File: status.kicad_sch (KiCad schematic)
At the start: 10 parts

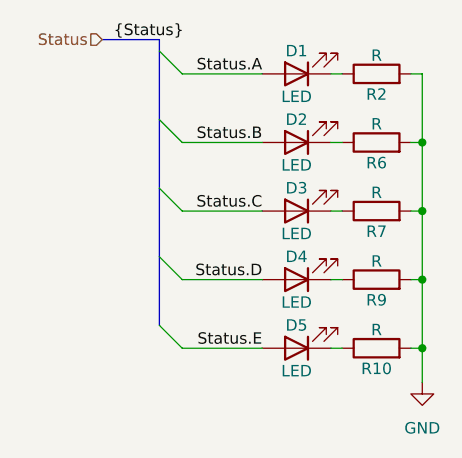
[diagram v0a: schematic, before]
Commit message: LED descriptions - Status LEDs could use some more work
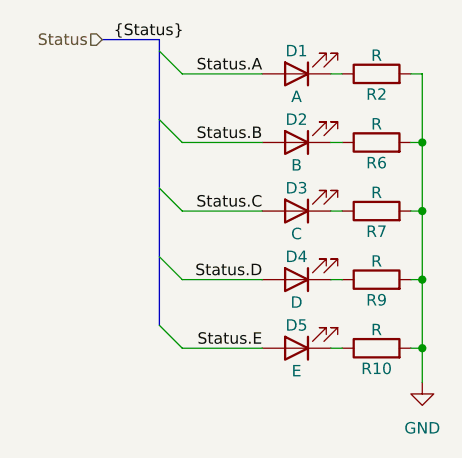
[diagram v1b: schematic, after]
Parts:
- D1: value LED -> A
- D2: value LED -> B
- D3: value LED -> C
- D4: value LED -> D
- D5: value LED -> E
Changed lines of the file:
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@@
 			)
 		)
-		(property "Value" "LED"
+		(property "Value" "B"
 			(at 140.97 95.25 0)
 			(effects
@@
 			)
 		)
-		(property "Value" "LED"
+		(property "Value" "C"
 			(at 140.97 102.87 0)
 			(effects
@@
 			)
 		)
-		(property "Value" "LED"
+		(property "Value" "E"
 			(at 140.97 118.11 0)
 			(effects
@@
 			)
 		)
-		(property "Value" "LED"
+		(property "Value" "D"
 			(at 140.97 110.49 0)
 			(effects
@@
 			)
 		)
-		(property "Value" "LED"
+		(property "Value" "A"
 			(at 140.97 87.63 0)
 			(effects

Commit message: Initial component placement
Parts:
- D1, D2, D3, D4, D5: footprint (none) -> LED_SMD:LED_0805_2012Metric_Pad1.15x1.40mm_HandSolder
- R10, R2, R6, R7, R9: footprint (none) -> Resistor_SMD:R_0805_2012Metric_Pad1.20x1.40mm_HandSolder
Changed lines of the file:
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@@
 			)
 		)
-		(property "Footprint" ""
+		(property "Footprint" "LED_SMD:LED_0805_2012Metric_Pad1.15x1.40mm_HandSolder"
 			(at 140.97 92.71 0)
 			(effects
@@
 			)
 		)
-		(property "Footprint" ""
+		(property "Footprint" "Resistor_SMD:R_0805_2012Metric_Pad1.20x1.40mm_HandSolder"
 			(at 149.86 117.348 90)
 			(effects
@@
 			)
 		)
-		(property "Footprint" ""
+		(property "Footprint" "Resistor_SMD:R_0805_2012Metric_Pad1.20x1.40mm_HandSolder"
 			(at 149.86 102.108 90)
 			(effects
@@
 			)
 		)
-		(property "Footprint" ""
+		(property "Footprint" "Resistor_SMD:R_0805_2012Metric_Pad1.20x1.40mm_HandSolder"
 			(at 149.86 94.488 90)
 			(effects
@@
 			)
 		)
-		(property "Footprint" ""
+		(property "Footprint" "Resistor_SMD:R_0805_2012Metric_Pad1.20x1.40mm_HandSolder"
 			(at 149.86 86.868 90)
 			(effects
@@
 			)
 		)
-		(property "Footprint" ""
+		(property "Footprint" "Resistor_SMD:R_0805_2012Metric_Pad1.20x1.40mm_HandSolder"
 			(at 149.86 109.728 90)
 			(effects
@@
 		(dnp no)
 		(fields_autoplaced yes)
-		(property "Reference" "#PWR016"
+		(property "Reference" "#PWR0101"
 			(at 154.94 125.73 0)
 			(effects
@@
 			(project "LifeCounter"
 				(path "/16b3e55a-9d75-49bf-a6fe-25414eb3d7da/2d968151-724a-4d29-815f-dbf368373ff9"
+					(reference "#PWR0101")
+					(unit 1)
+				)
+				(path "/16b3e55a-9d75-49bf-a6fe-25414eb3d7da/8c2171b0-d87d-41f8-af80-94d86e99ac21"
 					(reference "#PWR016")
 					(unit 1)
@@
 			)
 		)
-		(property "Footprint" ""
+		(property "Footprint" "LED_SMD:LED_0805_2012Metric_Pad1.15x1.40mm_HandSolder"
 			(at 140.97 100.33 0)
 			(effects
@@
 			)
 		)
-		(property "Footprint" ""
+		(property "Footprint" "LED_SMD:LED_0805_2012Metric_Pad1.15x1.40mm_HandSolder"
 			(at 140.97 115.57 0)
 			(effects
@@
 			)
 		)
-		(property "Footprint" ""
+		(property "Footprint" "LED_SMD:LED_0805_2012Metric_Pad1.15x1.40mm_HandSolder"
 			(at 140.97 107.95 0)
 			(effects
@@
 			)
 		)
-		(property "Footprint" ""
+		(property "Footprint" "LED_SMD:LED_0805_2012Metric_Pad1.15x1.40mm_HandSolder"
 			(at 140.97 85.09 0)
 			(effects

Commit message: Initial layout
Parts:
- renumbered D4 to D14, D5 to D15, D1 to D6, D2 to D7, D3 to D8, R2 to R26, R6 to R27, R7 to R28, R9 to R29, R10 to R30
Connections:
- net Status.A renamed A
- net Status.B renamed B
- net Status.C renamed C
- net Status.D renamed D
- net Status.E renamed E
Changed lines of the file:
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@@
 	)
 	(bus_entry
-		(at 125.73 97.79)
+		(at 132.08 97.79)
 		(size 2.54 2.54)
 		(stroke
@@
 	)
 	(bus_entry
-		(at 125.73 82.55)
+		(at 132.08 82.55)
 		(size 2.54 2.54)
 		(stroke
@@
 	)
 	(bus_entry
-		(at 125.73 113.03)
+		(at 132.08 113.03)
 		(size 2.54 2.54)
 		(stroke
@@
 	)
 	(bus_entry
-		(at 125.73 105.41)
+		(at 132.08 105.41)
 		(size 2.54 2.54)
 		(stroke
@@
 	)
 	(bus_entry
-		(at 125.73 90.17)
+		(at 132.08 90.17)
 		(size 2.54 2.54)
 		(stroke
@@
 	(wire
 		(pts
-			(xy 128.27 85.09) (xy 137.16 85.09)
+			(xy 134.62 85.09) (xy 137.16 85.09)
 		)
 		(stroke
@@
 	(wire
 		(pts
-			(xy 128.27 100.33) (xy 137.16 100.33)
-		)
-		(stroke
-			(width 0)
-			(type default)
-		)
-	)
-	(wire
-		(pts
-			(xy 128.27 107.95) (xy 137.16 107.95)
+			(xy 134.62 100.33) (xy 137.16 100.33)
+		)
+		(stroke
+			(width 0)
+			(type default)
+		)
+	)
+	(wire
+		(pts
+			(xy 134.62 107.95) (xy 137.16 107.95)
 		)
 		(stroke
@@
 	(wire
 		(pts
-			(xy 128.27 92.71) (xy 137.16 92.71)
+			(xy 134.62 92.71) (xy 137.16 92.71)
 		)
 		(stroke
@@
 	(bus
 		(pts
-			(xy 119.38 81.28) (xy 125.73 81.28)
+			(xy 125.73 81.28) (xy 132.08 81.28)
 		)
 		(stroke
@@
 	(bus
 		(pts
-			(xy 125.73 82.55) (xy 125.73 90.17)
+			(xy 132.08 82.55) (xy 132.08 90.17)
 		)
 		(stroke
@@
 	(bus
 		(pts
-			(xy 125.73 105.41) (xy 125.73 113.03)
+			(xy 132.08 105.41) (xy 132.08 113.03)
 		)
 		(stroke
@@
 	(bus
 		(pts
-			(xy 125.73 97.79) (xy 125.73 105.41)
+			(xy 132.08 97.79) (xy 132.08 105.41)
 		)
 		(stroke
@@
 	(bus
 		(pts
-			(xy 125.73 81.28) (xy 125.73 82.55)
-		)
-		(stroke
-			(width 0)
-			(type default)
-		)
-	)
-	(wire
-		(pts
-			(xy 128.27 115.57) (xy 137.16 115.57)
+			(xy 132.08 81.28) (xy 132.08 82.55)
+		)
+		(stroke
+			(width 0)
+			(type default)
+		)
+	)
+	(wire
+		(pts
+			(xy 134.62 115.57) (xy 137.16 115.57)
 		)
 		(stroke
@@
 	(bus
 		(pts
-			(xy 125.73 90.17) (xy 125.73 97.79)
+			(xy 132.08 90.17) (xy 132.08 97.79)
 		)
 		(stroke
@@
 		)
 	)
-	(label "Status.A"
+	(label "A"
 		(at 137.16 85.09 180)
 		(fields_autoplaced yes)
@@
 		)
 	)
-	(label "Status.E"
+	(label "E"
 		(at 137.16 115.57 180)
 		(fields_autoplaced yes)
@@
 		)
 	)
-	(label "Status.D"
+	(label "D"
 		(at 137.16 107.95 180)
 		(fields_autoplaced yes)
@@
 		)
 	)
-	(label "Status.C"
+	(label "C"
 		(at 137.16 100.33 180)
 		(fields_autoplaced yes)
@@
 	)
 	(label "{Status}"
-		(at 120.65 81.28 0)
+		(at 127 81.28 0)
 		(fields_autoplaced yes)
 		(effects
@@
 		)
 	)
-	(label "Status.B"
+	(label "B"
 		(at 137.16 92.71 180)
 		(fields_autoplaced yes)
@@
 	(hierarchical_label "Status"
 		(shape input)
-		(at 119.38 81.28 180)
+		(at 125.73 81.28 180)
 		(fields_autoplaced yes)
 		(effects
@@
 		(on_board yes)
 		(dnp no)
-		(property "Reference" "D2"
+		(property "Reference" "D7"
 			(at 140.97 90.17 0)
 			(effects
@@
 		(on_board yes)
 		(dnp no)
-		(property "Reference" "R10"
+		(property "Reference" "R30"
 			(at 149.86 117.856 90)
 			(effects
@@
 		(on_board yes)
 		(dnp no)
-		(property "Reference" "R7"
+		(property "Reference" "R28"
 			(at 149.86 102.616 90)
 			(effects
@@
 		(on_board yes)
 		(dnp no)
-		(property "Reference" "R6"
+		(property "Reference" "R27"
 			(at 149.86 94.996 90)
 			(effects
@@
 		(on_board yes)
 		(dnp no)
-		(property "Reference" "R2"
+		(property "Reference" "R26"
 			(at 149.86 87.376 90)
 			(effects
@@
 		(on_board yes)
 		(dnp no)
-		(property "Reference" "R9"
+		(property "Reference" "R29"
 			(at 149.86 110.236 90)
 			(effects
@@
 		(on_board yes)
 		(dnp no)
-		(property "Reference" "D3"
+		(property "Reference" "D8"
 			(at 140.97 97.79 0)
 			(effects
@@
 		(on_board yes)
 		(dnp no)
-		(property "Reference" "D5"
+		(property "Reference" "D15"
 			(at 140.97 113.03 0)
 			(effects
@@
 		(on_board yes)
 		(dnp no)
-		(property "Reference" "D4"
+		(property "Reference" "D14"
 			(at 140.97 105.41 0)
 			(effects
@@
 		(on_board yes)
 		(dnp no)
-		(property "Reference" "D1"
+		(property "Reference" "D6"
 			(at 140.97 82.55 0)
 			(effects

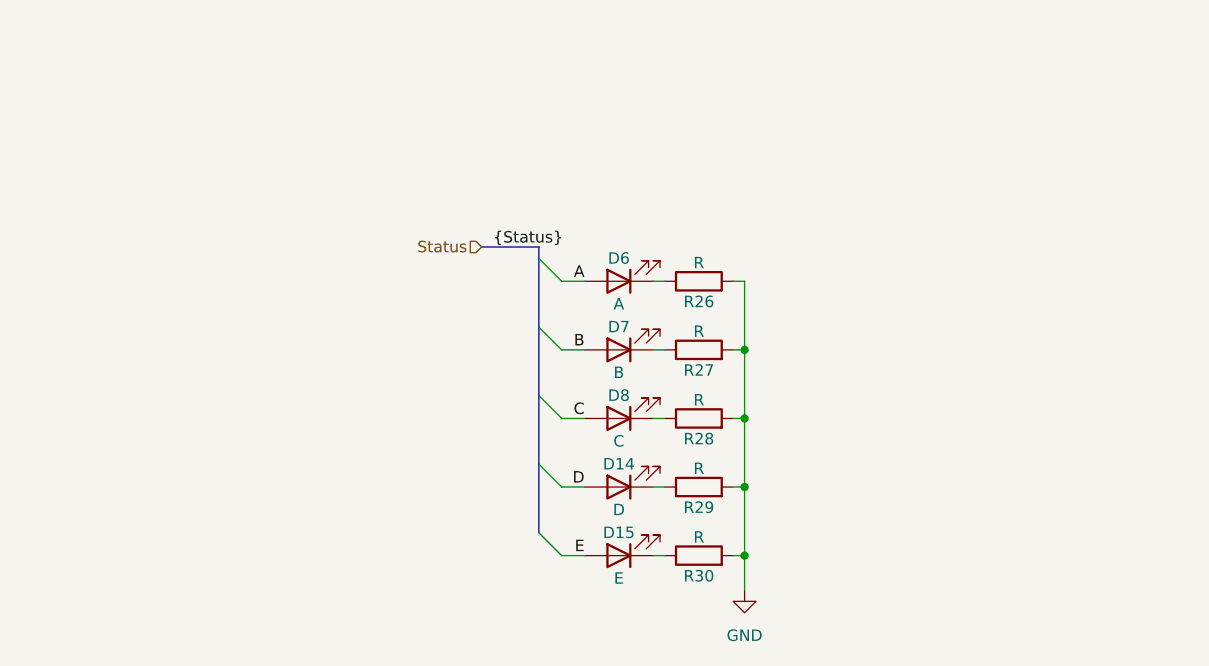
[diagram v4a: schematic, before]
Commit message: Constant current sink to status LEDs and rewiring controller
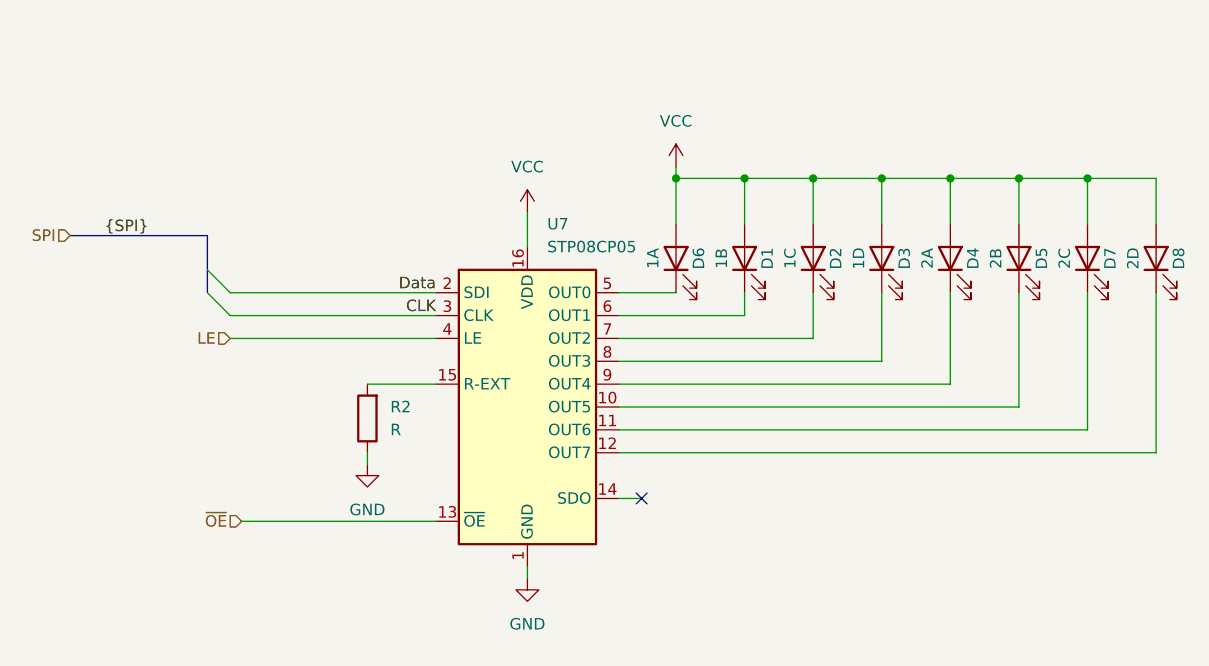
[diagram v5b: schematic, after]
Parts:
- removed D14: D, LED_SMD:LED_0805_2012Metric_Pad1.15x1.40mm_HandSolder, symbol Device:LED
- removed D15: E, LED_SMD:LED_0805_2012Metric_Pad1.15x1.40mm_HandSolder, symbol Device:LED
- removed R26, R27, R28, R29, R30: R, Resistor_SMD:R_0805_2012Metric_Pad1.20x1.40mm_HandSolder, symbol Device:R
- added D1: 1B, LED_SMD:LED_0805_2012Metric_Pad1.15x1.40mm_HandSolder, symbol Device:LED
- added D2: 1C, LED_SMD:LED_0805_2012Metric_Pad1.15x1.40mm_HandSolder, symbol Device:LED
- added D3: 1D, LED_SMD:LED_0805_2012Metric_Pad1.15x1.40mm_HandSolder, symbol Device:LED
- added D4: 2A, LED_SMD:LED_0805_2012Metric_Pad1.15x1.40mm_HandSolder, symbol Device:LED
- added D5: 2B, LED_SMD:LED_0805_2012Metric_Pad1.15x1.40mm_HandSolder, symbol Device:LED
- added R2: R, Resistor_SMD:R_0805_2012Metric_Pad1.20x1.40mm_HandSolder, symbol Device:R
- added U7: STP08CP05, symbol Driver_LED:STP08CP05
- D6: value A -> 1A
- D7: value B -> 2C
- D8: value C -> 2D
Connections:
- net B is gone; now on net VCC: D7.2 (A)
- net C is gone; now on net VCC: D8.2 (A)
- net GND: now also R2.1, U7.1 (GND)
- net at D7.1 (K): now also U7.11 (OUT6)
- net at D8.1 (K): now also U7.12 (OUT7)
- net at D6.1 (K): now also U7.5 (OUT0)
- net A renamed VCC
- net VCC: now also D1.2 (A), D2.2 (A), D3.2 (A), D4.2 (A), D5.2 (A), U7.16 (VDD)
- new net: D2.1 (K), U7.7 (OUT2)
- new net: D5.1 (K), U7.10 (OUT5)
- new net: D3.1 (K), U7.8 (OUT3)
- new net: D4.1 (K), U7.9 (OUT4)
- new net: R2.2, U7.15 (R-EXT)
- new net: D1.1 (K), U7.6 (OUT1)
- new net CLK: U7.3 (CLK)
- new net Data: U7.2 (SDI)
- new net LE: U7.4 (LE)
- new net ~{OE}: U7.13 (~{OE})
- no-connect marks 0 -> 1

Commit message: Status component value assignment
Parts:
- added C19: 100n, Capacitor_SMD:C_0805_2012Metric_Pad1.18x1.45mm_HandSolder, symbol Device:C
- added C20: 10u, Capacitor_SMD:C_0805_2012Metric_Pad1.18x1.45mm_HandSolder, symbol Device:C
- R2: value R -> 1k
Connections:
- net GND: now also C19.2, C20.2
- net VCC: now also C19.1, C20.1
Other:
- note added: "~3mA -> 6K7 ~5mA -> 4K ~10mA -> 2K ~20mA -> 1K ~50mA -> 400 ~80mA -> 220 ~130mA -> 120"

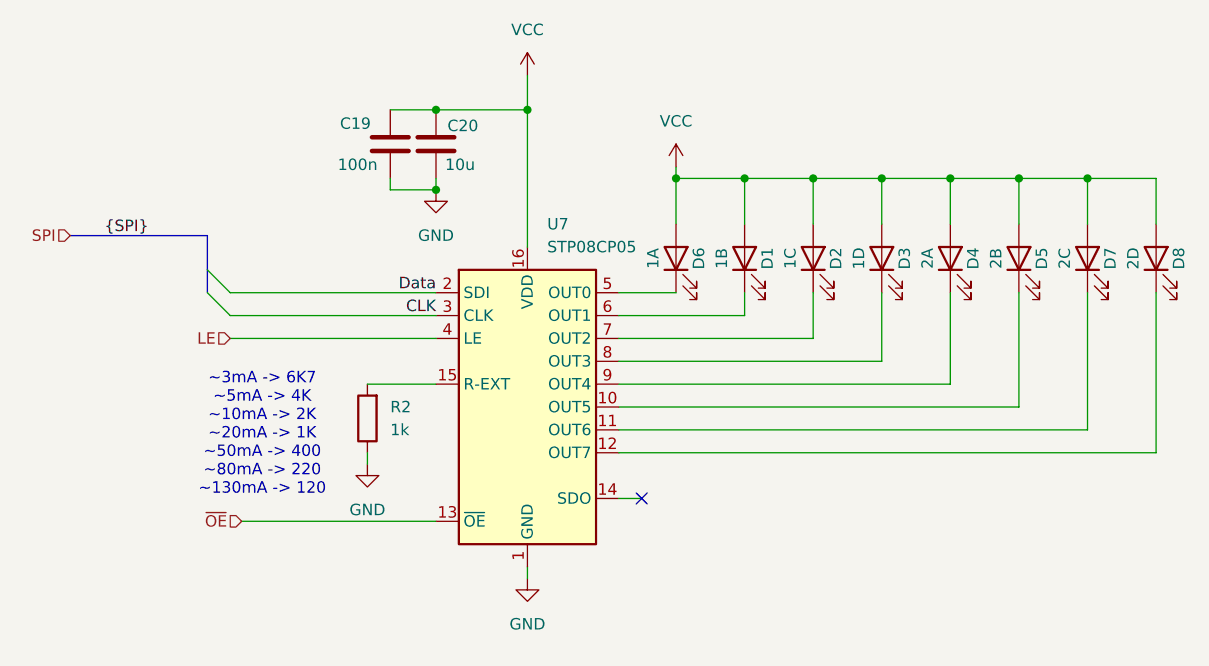
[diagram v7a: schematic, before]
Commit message: Decoupling capacitor change from 10u to 1u
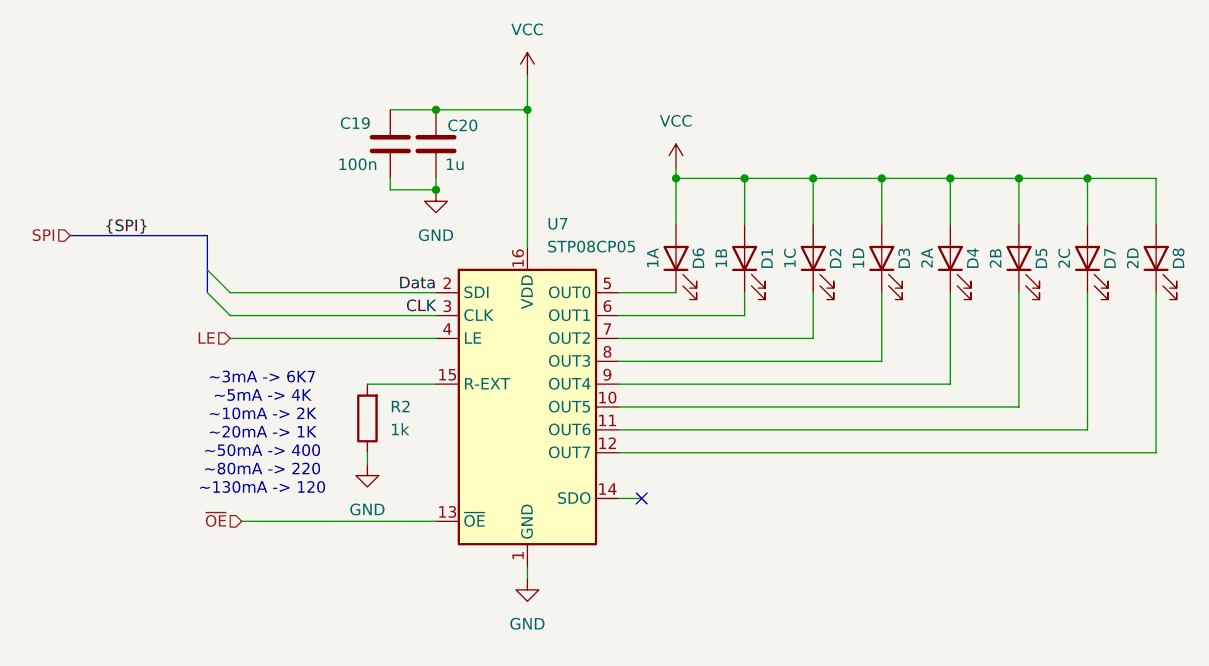
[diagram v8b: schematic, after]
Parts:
- C20: value 10u -> 1u
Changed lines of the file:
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@@
 			)
 		)
-		(property "Value" "10u"
+		(property "Value" "1u"
 			(at 121.666 72.136 0)
 			(effects
